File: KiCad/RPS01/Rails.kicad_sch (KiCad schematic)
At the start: 0 parts

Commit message: Updates
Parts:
- added J13, J14, J5: AMASS_XT60-F_1x02_P7.20mm_Vertical, Connector_AMASS:AMASS_XT60-F_1x02_P7.20mm_Vertical, symbol Connector:Conn_01x02_Socket
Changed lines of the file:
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@@
 (kicad_sch (version 20230121) (generator eeschema)
   (paper "A4")
+  (symbol (lib_id "Connector:Conn_01x02_Socket") (at 227.33 98.298 0) (unit 1)
+    (in_bom yes) (on_board yes) (dnp no) (fields_autoplaced)
+    (property "Reference" "J13" (at 228.6 98.933 0)
+      (effects (font (size 1.27 1.27)) (justify left))
+    )
+    (property "Value" "AMASS_XT60-F_1x02_P7.20mm_Vertical" (at 228.6 101.473 0)
+      (effects (font (size 1.27 1.27)) (justify left))
+    )
+    (property "Footprint" "Connector_AMASS:AMASS_XT60-F_1x02_P7.20mm_Vertical" (at 227.33 98.298 0)
+      (effects (font (size 1.27 1.27)) hide)
+    )
+    (property "Datasheet" "~" (at 227.33 98.298 0)
+      (effects (font (size 1.27 1.27)) hide)
+    )
+    (pin "1")
+    (pin "2")
+    (instances
+      (project "rps01"
+        (path "/14930f15-c0a0-4b55-93e6-b112548415f6/6ed54b0f-f89c-4a82-b1ab-c92c0c126d05"
+          (reference "J13") (unit 1)
+        )
+      )
+    )
+  )
+  (symbol (lib_id "Connector:Conn_01x02_Socket") (at 226.822 116.078 0) (unit 1)
+    (in_bom yes) (on_board yes) (dnp no) (fields_autoplaced)
+    (property "Reference" "J14" (at 228.6 116.713 0)
+      (effects (font (size 1.27 1.27)) (justify left))
+    )
+    (property "Value" "AMASS_XT60-F_1x02_P7.20mm_Vertical" (at 228.6 119.253 0)
+      (effects (font (size 1.27 1.27)) (justify left))
+    )
+    (property "Footprint" "Connector_AMASS:AMASS_XT60-F_1x02_P7.20mm_Vertical" (at 226.822 116.078 0)
+      (effects (font (size 1.27 1.27)) hide)
+    )
+    (property "Datasheet" "~" (at 226.822 116.078 0)
+      (effects (font (size 1.27 1.27)) hide)
+    )
+    (pin "1")
+    (pin "2")
+    (instances
+      (project "rps01"
+        (path "/14930f15-c0a0-4b55-93e6-b112548415f6/6ed54b0f-f89c-4a82-b1ab-c92c0c126d05"
+          (reference "J14") (unit 1)
+        )
+      )
+    )
+  )
+  (symbol (lib_id "Connector:Conn_01x02_Socket") (at 227.584 80.772 0) (unit 1)
+    (in_bom yes) (on_board yes) (dnp no) (fields_autoplaced)
+    (property "Reference" "J5" (at 228.6 81.407 0)
+      (effects (font (size 1.27 1.27)) (justify left))
+    )
+    (property "Value" "AMASS_XT60-F_1x02_P7.20mm_Vertical" (at 228.6 83.947 0)
+      (effects (font (size 1.27 1.27)) (justify left))
+    )
+    (property "Footprint" "Connector_AMASS:AMASS_XT60-F_1x02_P7.20mm_Vertical" (at 227.584 80.772 0)
+      (effects (font (size 1.27 1.27)) hide)
+    )
+    (property "Datasheet" "~" (at 227.584 80.772 0)
+      (effects (font (size 1.27 1.27)) hide)
+    )
+    (pin "1")
+    (pin "2")
+    (instances
+      (project "rps01"
+        (path "/14930f15-c0a0-4b55-93e6-b112548415f6/6ed54b0f-f89c-4a82-b1ab-c92c0c126d05"
+          (reference "J5") (unit 1)
+        )
+      )
+    )
+  )
 )

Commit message: Large Schematic Update
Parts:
- removed J13, J14, J5: AMASS_XT60-F_1x02_P7.20mm_Vertical, Connector_AMASS:AMASS_XT60-F_1x02_P7.20mm_Vertical, symbol Connector:Conn_01x02_Socket
- added U2: AMS1117, Package_TO_SOT_SMD:SOT-223-3_TabPin2, symbol Regulator_Linear:AMS1117
- added U9: L78M05CDT-TR 5V Reg, Mechatronic Footprints:5V_REGULATOR_DPAK_STM, symbol 5V Regulator:L78M05CDT-TR
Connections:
- new net +5V: U9.2 (OUTPUT)
- new net +BATT: U9.1 (INPUT)
- new net GND: U2.1 (ADJ), U9.3 (GROUND)

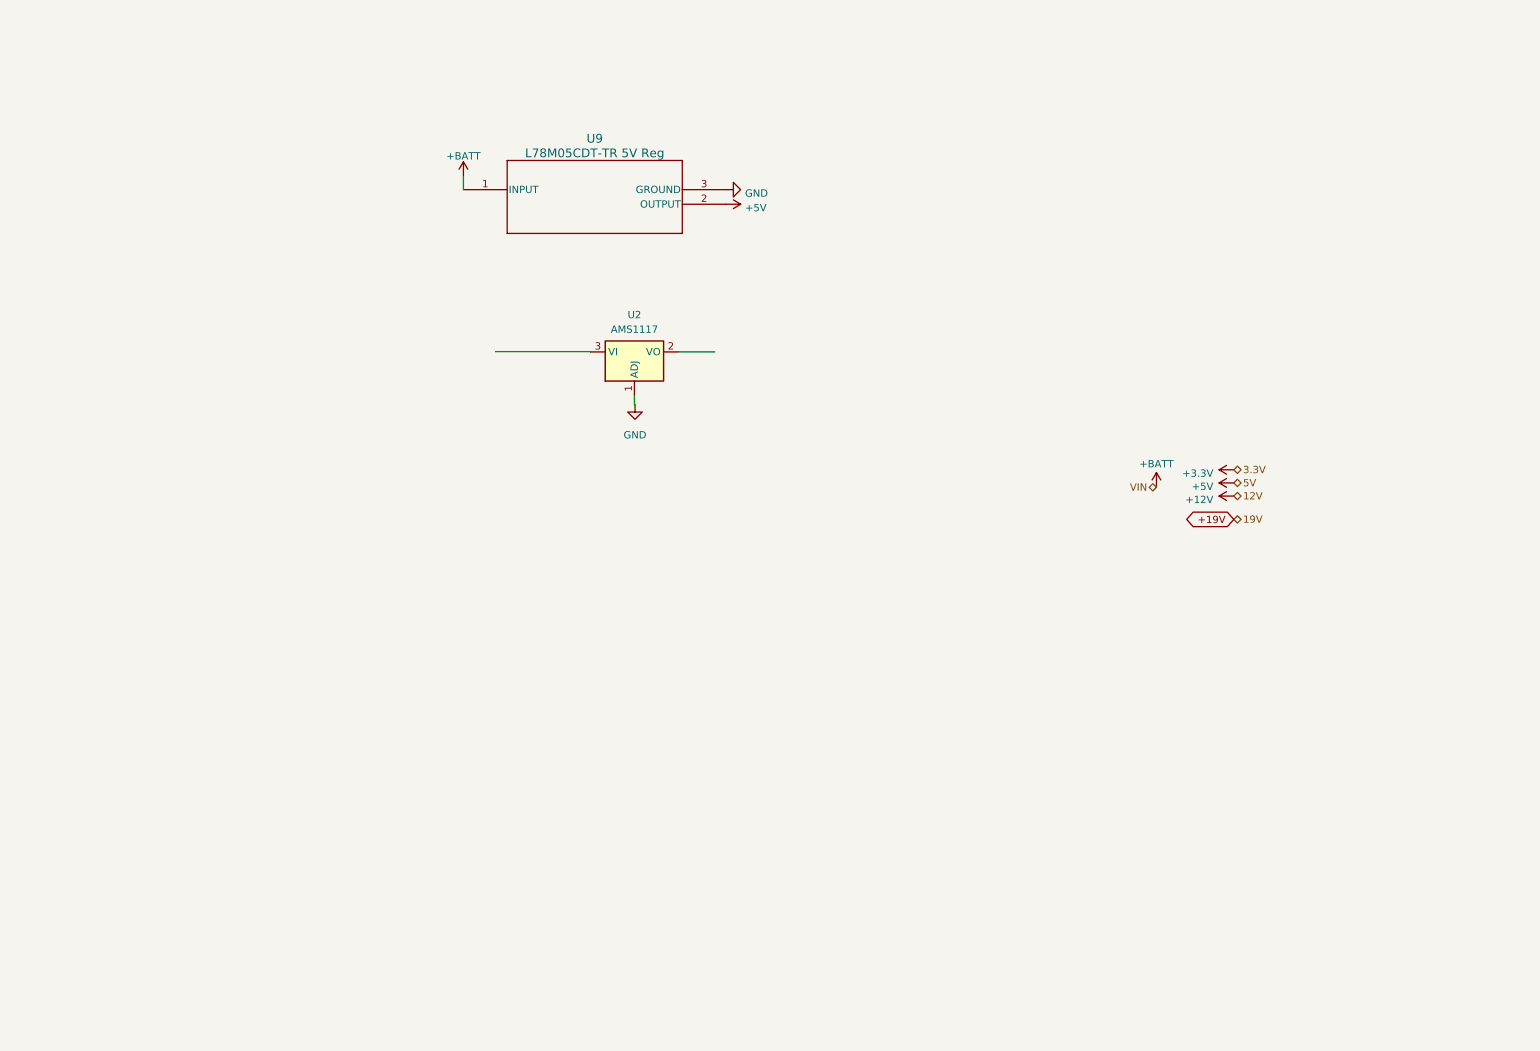
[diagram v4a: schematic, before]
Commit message: Finished most of the Schematics. Needs polishing
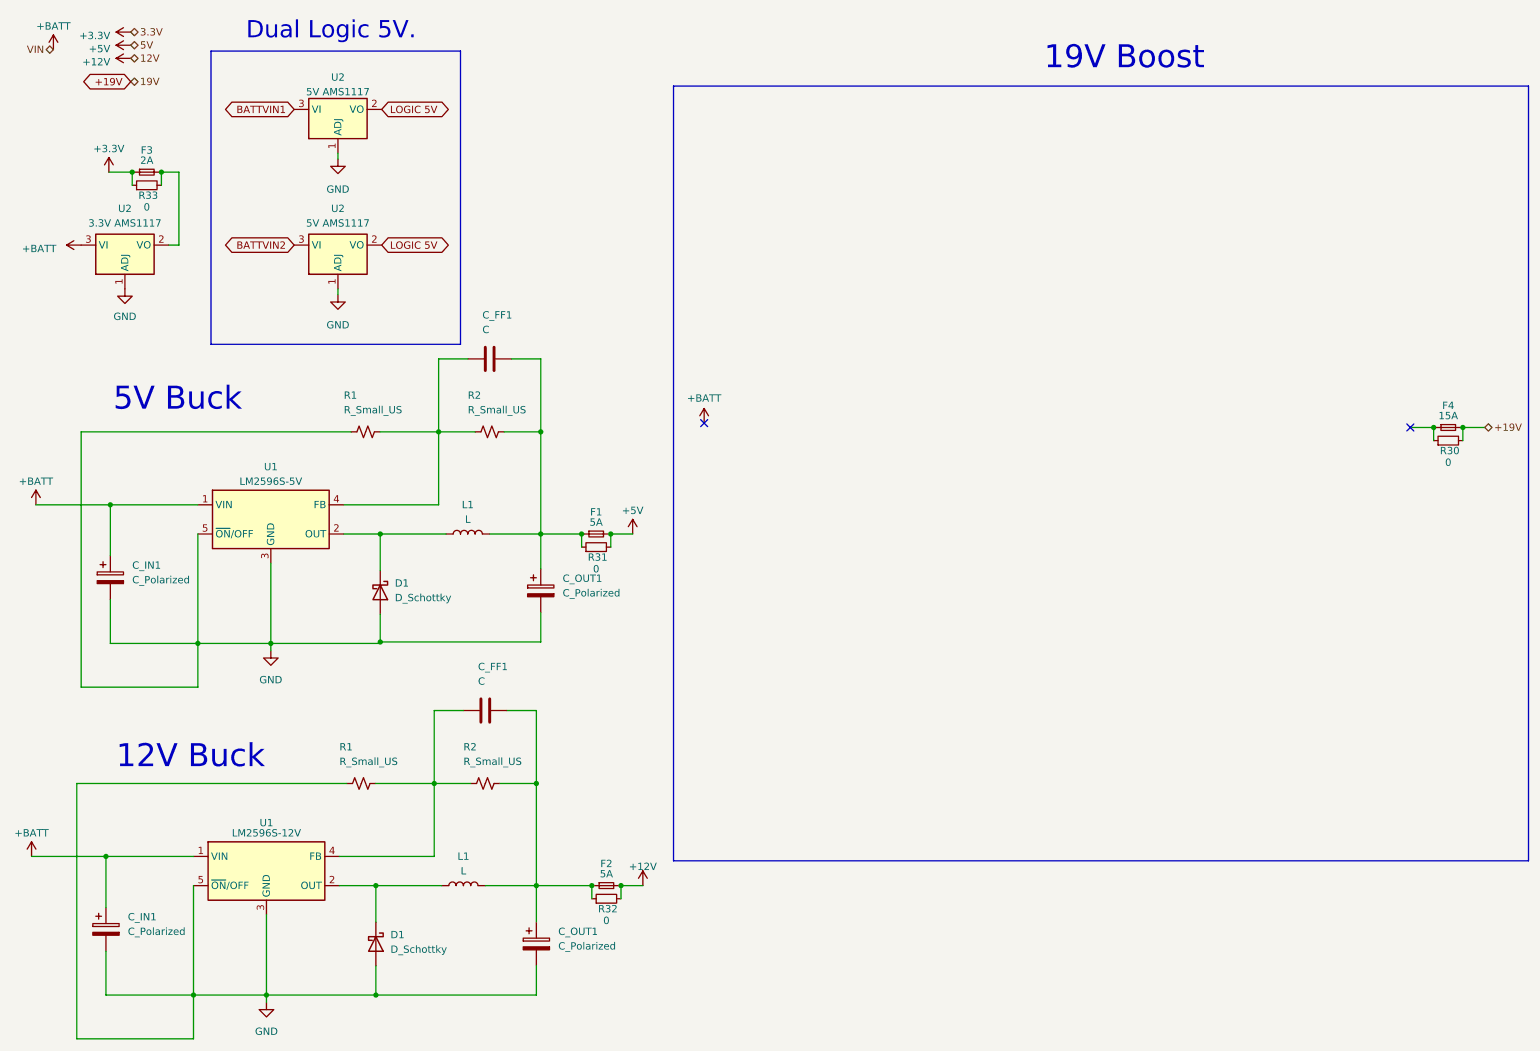
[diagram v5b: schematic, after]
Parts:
- removed U9: L78M05CDT-TR 5V Reg, Mechatronic Footprints:5V_REGULATOR_DPAK_STM, symbol 5V Regulator:L78M05CDT-TR
- added C_FF1 (x2): C, Capacitor_SMD:C_1206_3216Metric, symbol Device:C
- added C_IN1 (x2), C_OUT1 (x2): C_Polarized, Capacitor_SMD:CP_Elec_8x10, symbol Device:C_Polarized
- added D1 (x2): D_Schottky, Mechatronic Footprints:CR_SMA_320-340AE_DIO, symbol Device:D_Schottky
- added F1, F2: 5A, symbol Device:Fuse_Small
- added F3: 2A, symbol Device:Fuse_Small
- added F4: 15A, symbol Device:Fuse_Small
- added L1 (x2): L, CDRH127_LDNP-470MC:IND_CDRH127_LDNP-470MC_SUM, symbol Device:L
- added R1 (x2), R2 (x2): R_Small_US, Resistor_SMD:R_1206_3216Metric, symbol Device:R_Small_US
- added R30, R31, R32, R33: 0, symbol Device:R_Small
- added U1: LM2596S-12V, Package_TO_SOT_SMD:TO-263-5_TabPin3, symbol Regulator_Switching:LM2596S-ADJ
- added U1: LM2596S-5V, Package_TO_SOT_SMD:TO-263-5_TabPin3, symbol Regulator_Switching:LM2596S-ADJ
- added U2: 3.3V AMS1117, Package_TO_SOT_SMD:SOT-223-3_TabPin2, symbol Regulator_Linear:AMS1117
- added U2: 5V AMS1117, Package_TO_SOT_SMD:SOT-223-3_TabPin2, symbol Regulator_Linear:AMS1117
- U2: value AMS1117 -> 5V AMS1117
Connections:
- net +12V: now also F2.2, R32.2
- net +19V: now also F4.2, R30.2
- net +3.3V: now also F3.1, R33.1
- net +5V: now also F1.2, R31.2
- net +BATT: now also C_IN1.1, C_IN1.1, U1.1 (VIN), U1.1 (VIN), U2.3 (VI)
- net GND: now also C_IN1.2, C_IN1.2, C_OUT1.2, C_OUT1.2, D1.2 (A), D1.2 (A), R1.1, R1.1, U1.3 (GND), U1.3 (GND), U1.5 (~{ON}/OFF), U1.5 (~{ON}/OFF), U2.1 (ADJ), U2.1 (ADJ)
- net LOGIC 5V: now reaches U2.2 (VO)
- net LOGIC 5V: now also U2.2 (VO)
- net BATTVIN1: now reaches U2.3 (VI)
- new net: F3.2, R33.2, U2.2 (VO)
- new net: C_FF1.2, C_OUT1.1, F1.1, L1.2, R2.2, R31.1
- new net: C_FF1.2, C_OUT1.1, F2.1, L1.2, R2.2, R32.1
- new net: F4.1, R30.1
- new net: D1.1 (K), L1.1, U1.2 (OUT) (x2)
- new net: C_FF1.1, R1.2, R2.1, U1.4 (FB) (x2)
- new net BATTVIN2: U2.3 (VI)
- no-connect marks 0 -> 2
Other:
- note added: "12V Buck"
- note added: "19V Boost"
- note added: "5V Buck"
- note added: "Dual Logic 5V."
- moved on the sheet: U2

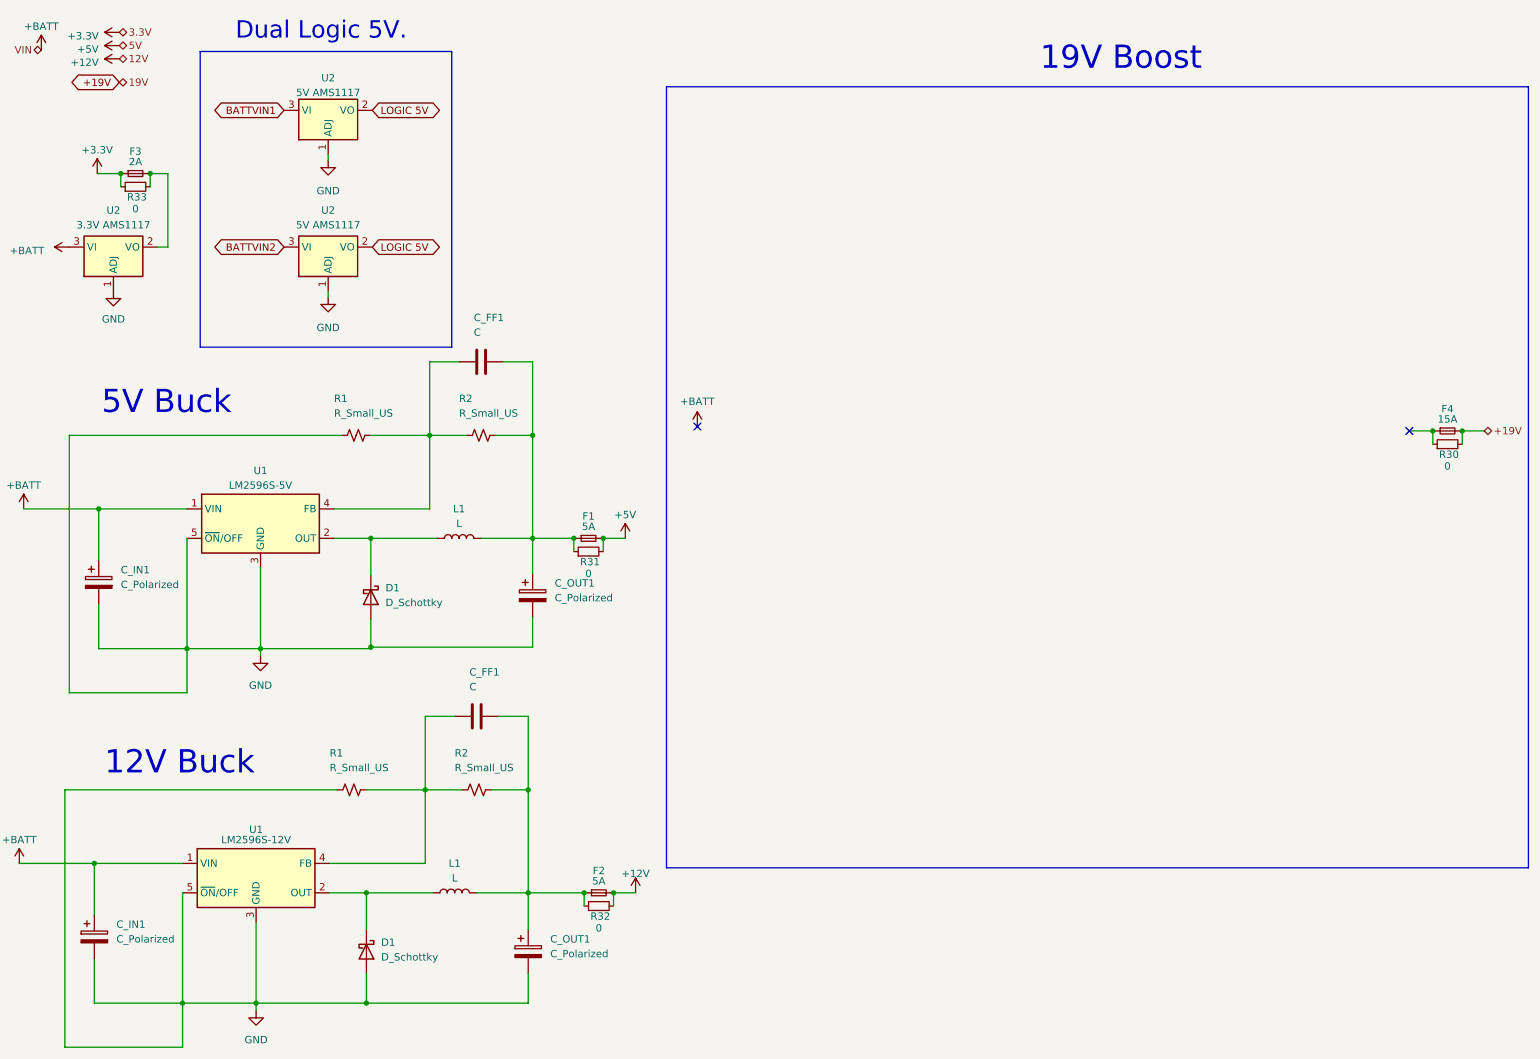
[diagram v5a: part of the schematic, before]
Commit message: Finished Updating Footprints and Reorganized Reference Designators
Finished Updating Footprints and Reorganized Reference Designators

Starting to work on Final PCB, except for 19V Boost. Please check Schematic for errors
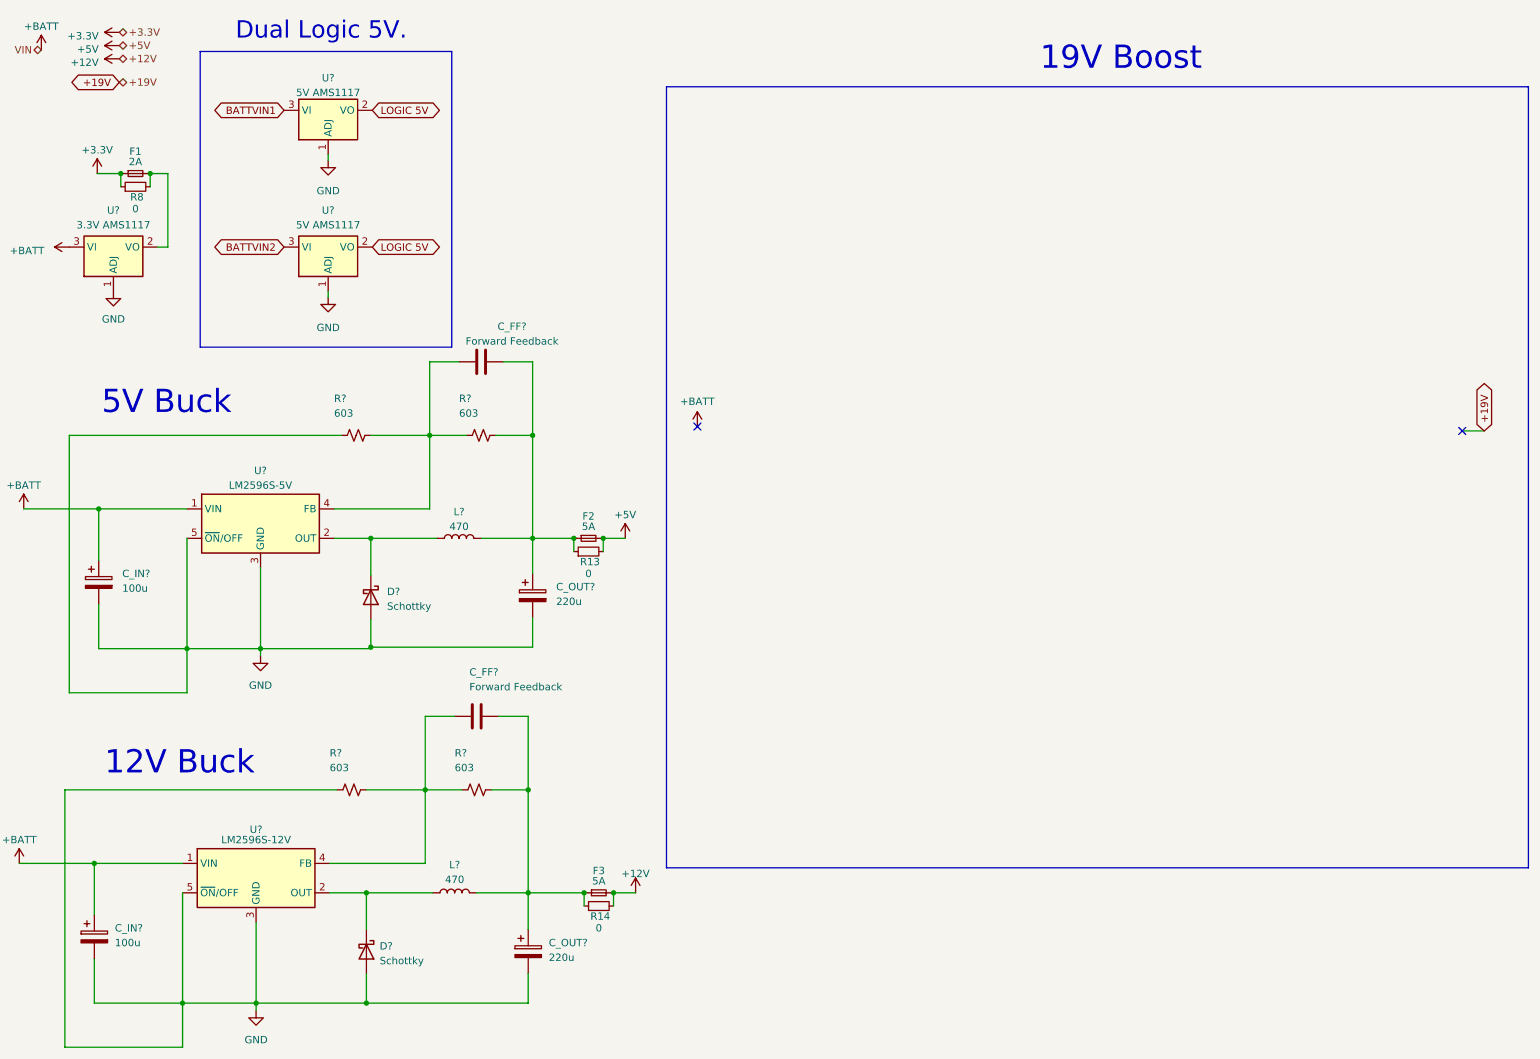
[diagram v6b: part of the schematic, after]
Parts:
- removed F4: 15A, symbol Device:Fuse_Small
- removed R30: 0, symbol Device:R_Small
- C_FF? (x2): renamed from C_FF1; value C -> Forward Feedback; footprint Capacitor_SMD:C_1206_3216Metric -> Capacitor_SMD:C_0603_1608Metric
- C_IN? (x2): renamed from C_IN1; value C_Polarized -> 100u
- C_OUT? (x2): renamed from C_OUT1; value C_Polarized -> 220u
- D? (x2): renamed from D1; value D_Schottky -> Schottky
- F1: renamed from F3; footprint (none) -> Mechatronics Fuses:0154Series_LTF
- F2: renamed from F1; footprint (none) -> Mechatronics Fuses:0154Series_LTF
- F3: renamed from F2; footprint (none) -> Mechatronics Fuses:0154Series_LTF
- L? (x2): renamed from L1; value L -> 470; footprint CDRH127_LDNP-470MC:IND_CDRH127_LDNP-470MC_SUM -> Mechatronics BUCK INDUCTOR:IND_CDRH127&slash_LDNP-470MC_SUM
- R13: renamed from R31; footprint (none) -> Resistor_SMD:R_0603_1608Metric
- R14: renamed from R32; footprint (none) -> Resistor_SMD:R_0603_1608Metric
- R8: renamed from R33; footprint (none) -> Resistor_SMD:R_0603_1608Metric
- R? (x2): renamed from R1; value R_Small_US -> 603
- R? (x2): renamed from R2; value R_Small_US -> 603
- renumbered U2 to U?, U1 to U?

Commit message: add resistor and cap values for buck
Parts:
- C_FF?: value Forward Feedback -> 3.3nF
- C_FF?: value Forward Feedback -> 10.75nF
- R? (x2): value 603 -> 1k
- R?: value 603 -> 9.75k
- R?: value 603 -> 3k
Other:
- note added: "603 package"
- note added: "Forward feedback"
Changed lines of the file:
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@@
     (fill (type none))
+  )
+  (text "Forward feedback" (at 102.87 132.08 0)
+    (effects (font (size 1.27 1.27)) (justify left bottom))
   )
   (text "19V Boost" (at 194.056 25.654 0)
     (effects (font (size 4 4)) (justify left bottom))
+  )
+  (text "603 package" (at 91.44 92.71 0)
+    (effects (font (size 1.27 1.27)) (justify left bottom))
+  )
+  (text "603 package" (at 69.85 152.4 0)
+    (effects (font (size 1.27 1.27)) (justify left bottom))
+  )
+  (text "603 package" (at 90.17 152.4 0)
+    (effects (font (size 1.27 1.27)) (justify left bottom))
+  )
+  (text "603 package" (at 71.12 92.71 0)
+    (effects (font (size 1.27 1.27)) (justify left bottom))
+  )
+  (text "Forward feedback" (at 107.95 72.39 0)
+    (effects (font (size 1.27 1.27)) (justify left bottom))
   )
   (text "5V Buck\n" (at 32.004 85.09 0)
@@
       (effects (font (size 1.27 1.27)) (justify right))
     )
-    (property "Value" "Forward Feedback" (at 95.504 131.826 90)
+    (property "Value" "3.3nF" (at 95.504 131.826 90)
       (effects (font (size 1.27 1.27)) (justify right))
     )
@@
       (effects (font (size 1.27 1.27)))
     )
-    (property "Value" "Forward Feedback" (at 102.87 72.136 90)
+    (property "Value" "10.75nF" (at 102.87 72.136 90)
       (effects (font (size 1.27 1.27)))
     )
@@
       (effects (font (size 1.27 1.27)) (justify right))
     )
-    (property "Value" "603" (at 72.136 84.582 90)
+    (property "Value" "1k" (at 72.136 84.582 90)
       (effects (font (size 1.27 1.27)) (justify right))
     )
@@
       (effects (font (size 1.27 1.27)) (justify right))
     )
-    (property "Value" "603" (at 92.964 145.796 90)
+    (property "Value" "9.75k" (at 92.964 145.796 90)
       (effects (font (size 1.27 1.27)) (justify right))
     )
@@
       (effects (font (size 1.27 1.27)) (justify right))
     )
-    (property "Value" "603" (at 71.374 145.796 90)
+    (property "Value" "1k" (at 71.374 145.796 90)
       (effects (font (size 1.27 1.27)) (justify right))
     )
@@
       (effects (font (size 1.27 1.27)) (justify right))
     )
-    (property "Value" "603" (at 93.726 84.582 90)
+    (property "Value" "3k" (at 93.726 84.582 90)
       (effects (font (size 1.27 1.27)) (justify right))
     )
